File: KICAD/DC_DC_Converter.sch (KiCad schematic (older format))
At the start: 0 parts

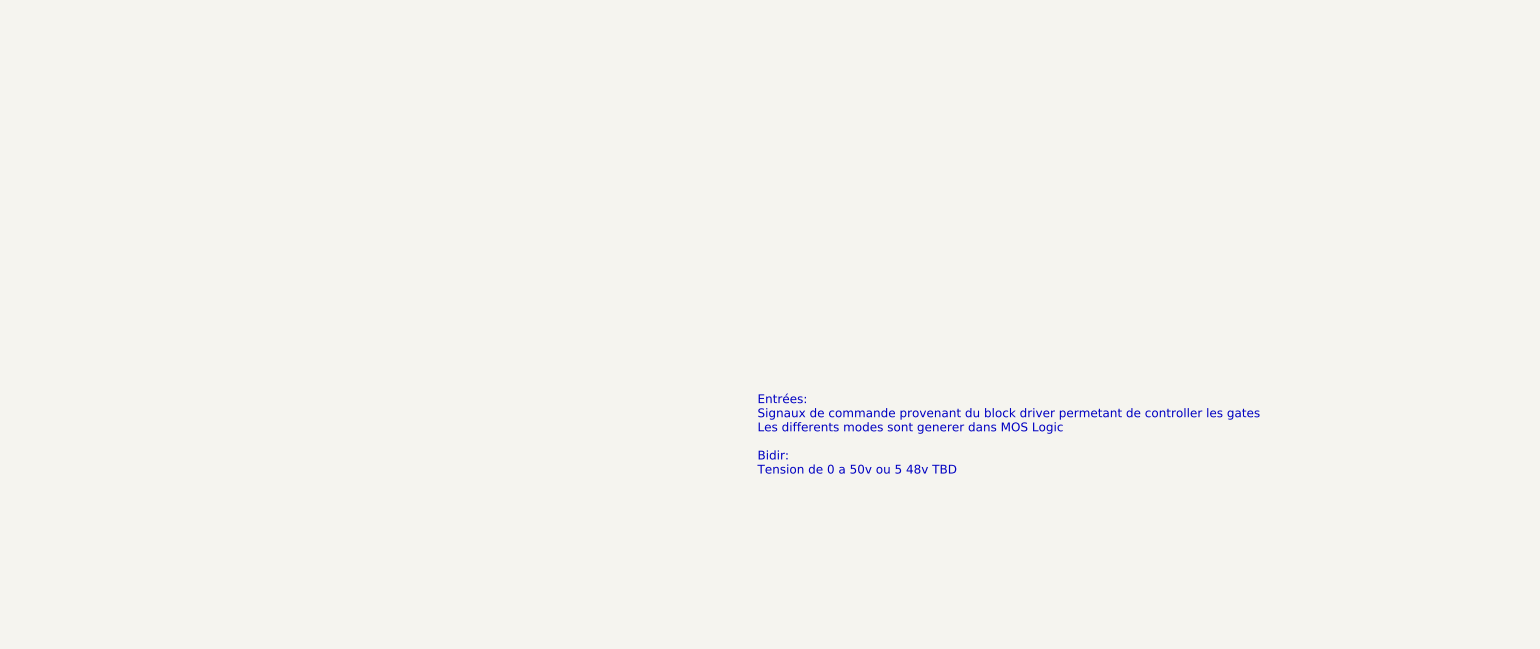
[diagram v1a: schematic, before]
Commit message: labels dans les blocks
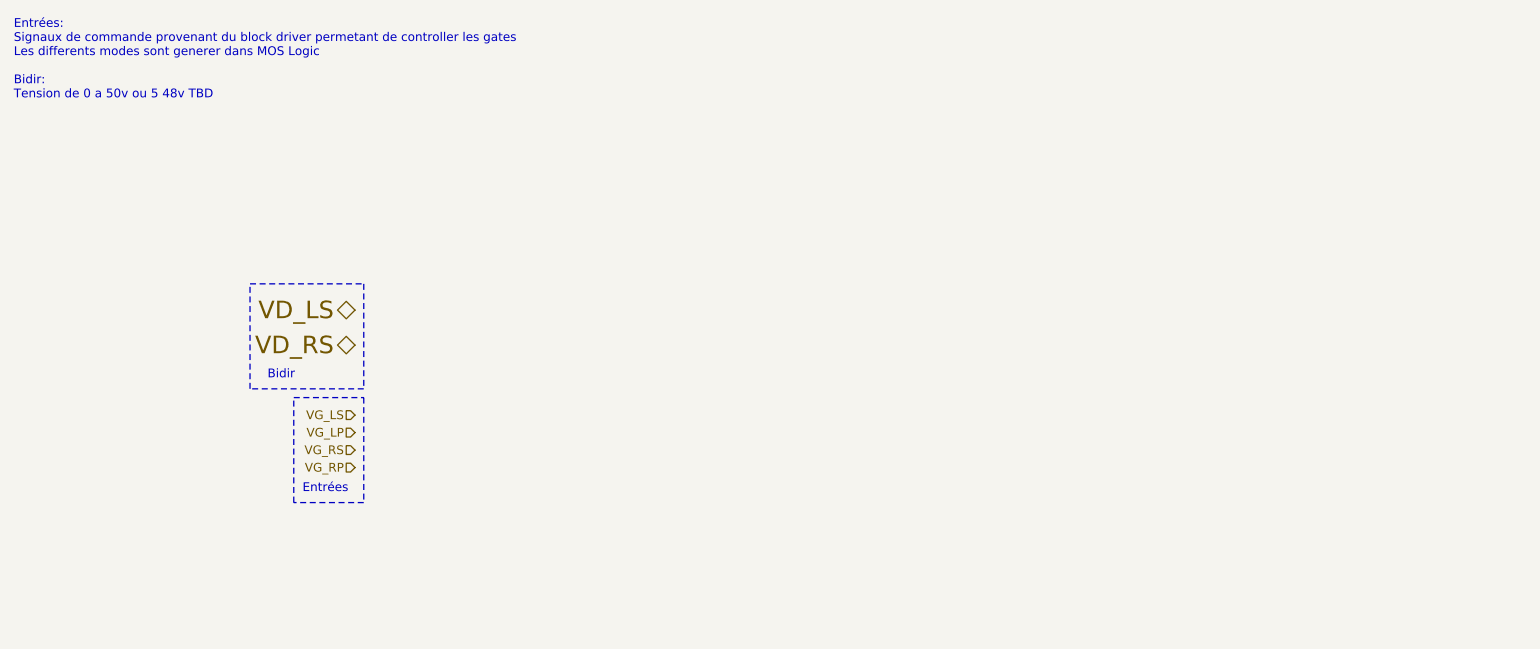
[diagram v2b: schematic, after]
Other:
- note added: "Bidir"
- note added: "Entrées"
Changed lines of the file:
@@
 Comment4 ""
 $EndDescr
-Text Notes 4800 3150 0    50   ~ 0
+Text Notes 550  1000 0    50   ~ 0
 Entrées:\nSignaux de commande provenant du block driver permetant de controller les gates\nLes differents modes sont generer dans MOS Logic\n\nBidir:\nTension de 0 a 50v ou 5 48v TBD\n
+Text HLabel 2500 2200 0    100  BiDi ~ 0
+VD_LS
+Text HLabel 2500 2400 0    100  BiDi ~ 0
+VD_RS
+Text HLabel 2500 2800 0    50   Input ~ 0
+VG_LS
+Text HLabel 2500 2900 0    50   Input ~ 0
+VG_LP
+Text HLabel 2500 3000 0    50   Input ~ 0
+VG_RS
+Text HLabel 2500 3100 0    50   Input ~ 0
+VG_RP
+Text Notes 2200 3250 0    50   ~ 0
+Entrées
+Text Notes 2000 2600 0    50   ~ 0
+Bidir
+Wire Notes Line
+	2550 3300 2150 3300
+Wire Notes Line
+	2150 3300 2150 2700
+Wire Notes Line
+	2150 2700 2550 2700
+Wire Notes Line
+	2550 2700 2550 3300
+Wire Notes Line
+	2550 2650 1900 2650
+Wire Notes Line
+	1900 2650 1900 2050
+Wire Notes Line
+	1900 2050 2550 2050
+Wire Notes Line
+	2550 2050 2550 2650
 $EndSCHEMATC

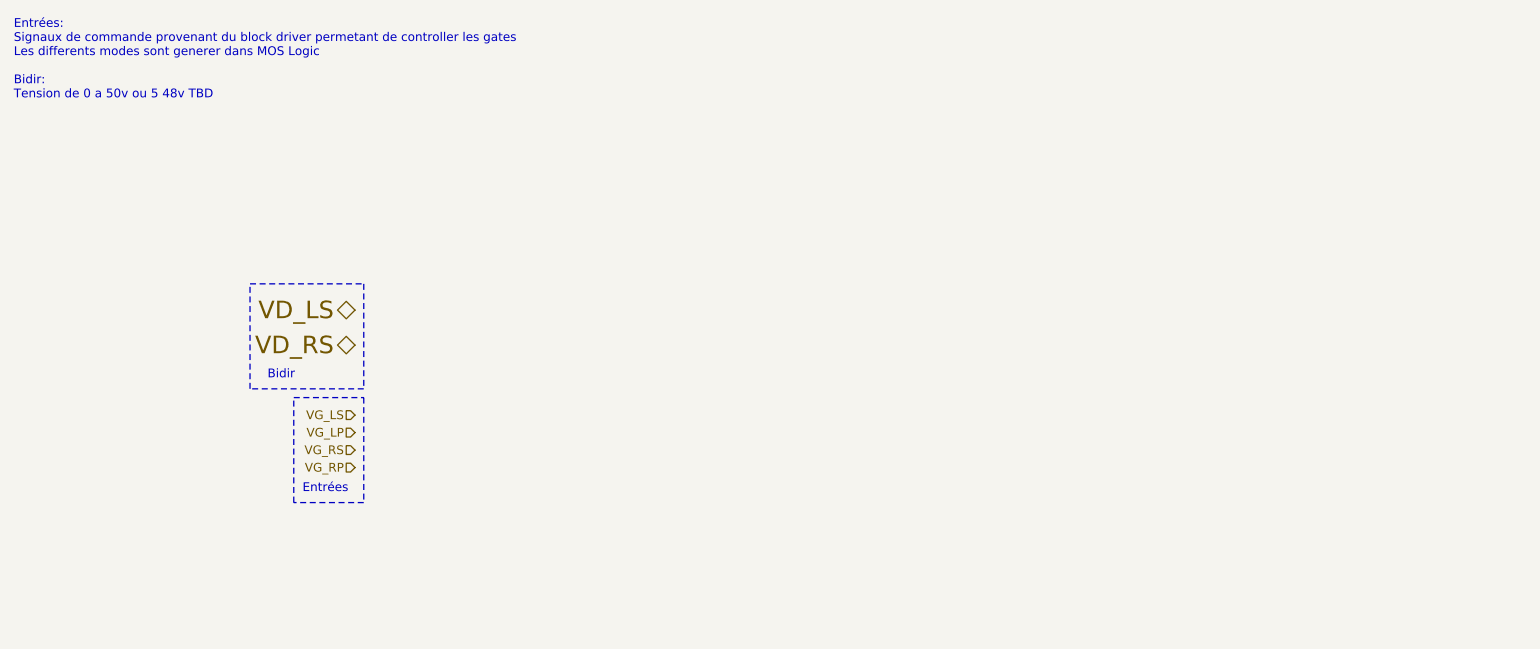
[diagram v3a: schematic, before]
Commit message: added ina240 sim + drawed protect and DC-DC chopper
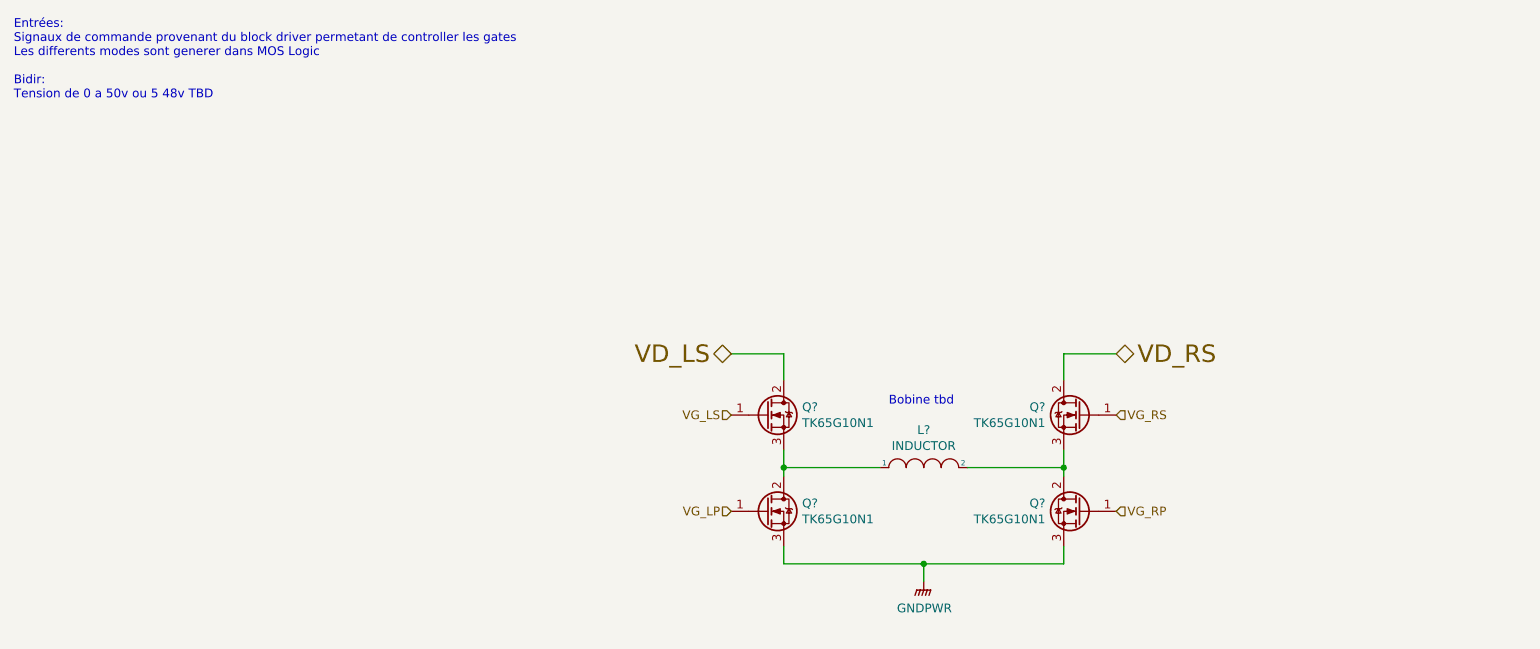
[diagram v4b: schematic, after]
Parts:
- added L?: INDUCTOR, symbol pspice:INDUCTOR
- added Q? (x4): TK65G10N1, symbol Device:Q_NMOS_GDS
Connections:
- net VD_LS: now also Q?.2 (D)
- net VD_RS: now also Q?.2 (D)
- net VG_LP: now also Q?.1 (G)
- net VG_LS: now also Q?.1 (G)
- net VG_RP: now also Q?.1 (G)
- net VG_RS: now also Q?.1 (G)
- new net: L?.1, Q?.2 (D), Q?.3 (S)
- new net: L?.2, Q?.2 (D), Q?.3 (S)
- new net GNDPWR: Q?.3 (S), Q?.3 (S)
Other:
- note added: "Bobine tbd"
- note removed: "Bidir"
- note removed: "Entrées"
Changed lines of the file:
@@
 Rev ""
 Comp "ALEEA"
-Comment1 ""
+Comment1 "Dessin : Guillaume Arthaud"
 Comment2 ""
 Comment3 ""
@@
 Text Notes 550  1000 0    50   ~ 0
 Entrées:\nSignaux de commande provenant du block driver permetant de controller les gates\nLes differents modes sont generer dans MOS Logic\n\nBidir:\nTension de 0 a 50v ou 5 48v TBD\n
-Text HLabel 2500 2200 0    100  BiDi ~ 0
+Text HLabel 4650 2450 0    100  BiDi ~ 0
 VD_LS
-Text HLabel 2500 2400 0    100  BiDi ~ 0
+Text HLabel 6850 2450 2    100  BiDi ~ 0
 VD_RS
-Text HLabel 2500 2800 0    50   Input ~ 0
+Text HLabel 4650 2800 0    50   Input ~ 0
 VG_LS
-Text HLabel 2500 2900 0    50   Input ~ 0
+Text HLabel 4650 3350 0    50   Input ~ 0
 VG_LP
-Text HLabel 2500 3000 0    50   Input ~ 0
+Text HLabel 6850 2800 2    50   Input ~ 0
 VG_RS
-Text HLabel 2500 3100 0    50   Input ~ 0
+Text HLabel 6850 3350 2    50   Input ~ 0
 VG_RP
-Text Notes 2200 3250 0    50   ~ 0
-Entrées
-Text Notes 2000 2600 0    50   ~ 0
-Bidir
-Wire Notes Line
-	2550 3300 2150 3300
-Wire Notes Line
-	2150 3300 2150 2700
-Wire Notes Line
-	2150 2700 2550 2700
-Wire Notes Line
-	2550 2700 2550 3300
-Wire Notes Line
-	2550 2650 1900 2650
-Wire Notes Line
-	1900 2650 1900 2050
-Wire Notes Line
-	1900 2050 2550 2050
-Wire Notes Line
-	2550 2050 2550 2650
+$Comp
+L Device:Q_NMOS_GDS Q?
+U 1 1 610E334F
+P 4850 2800
+F 0 "Q?" H 5055 2846 50  0000 L CNN
+F 1 "TK65G10N1" H 5055 2755 50  0000 L CNN
+F 2 "" H 5050 2900 50  0001 C CNN
+F 3 "~" H 4850 2800 50  0001 C CNN
+	1    4850 2800
+	1    0    0    -1
+$EndComp
+$Comp
+L Device:Q_NMOS_GDS Q?
+U 1 1 610EEE2E
+P 4850 3350
+F 0 "Q?" H 5055 3396 50  0000 L CNN
+F 1 "TK65G10N1" H 5055 3305 50  0000 L CNN
+F 2 "" H 5050 3450 50  0001 C CNN
+F 3 "~" H 4850 3350 50  0001 C CNN
+	1    4850 3350
+	1    0    0    -1
+$EndComp
+$Comp
+L Device:Q_NMOS_GDS Q?
+U 1 1 610F207F
+P 6650 2800
+F 0 "Q?" H 6855 2846 50  0000 L CNN
+F 1 "TK65G10N1" H 6855 2755 50  0000 L CNN
+F 2 "" H 6850 2900 50  0001 C CNN
+F 3 "~" H 6650 2800 50  0001 C CNN
+	1    6650 2800
+	-1   0    0    -1
+$EndComp
+$Comp
+L Device:Q_NMOS_GDS Q?
+U 1 1 610F2085
+P 6650 3350
+F 0 "Q?" H 6855 3396 50  0000 L CNN
+F 1 "TK65G10N1" H 6855 3305 50  0000 L CNN
+F 2 "" H 6850 3450 50  0001 C CNN
+F 3 "~" H 6650 3350 50  0001 C CNN
+	1    6650 3350
+	-1   0    0    -1
+$EndComp
+Wire Wire Line
+	6550 3000 6550 3100
+Wire Wire Line
+	4950 3150 4950 3100
+Wire Wire Line
+	4950 3550 4950 3650
+Wire Wire Line
+	6550 3650 6550 3550
+$Comp
+L pspice:INDUCTOR L?
+U 1 1 610F3EF5
+P 5750 3100
+F 0 "L?" H 5750 3315 50  0000 C CNN
+F 1 "INDUCTOR" H 5750 3224 50  0000 C CNN
+F 2 "" H 5750 3100 50  0001 C CNN
+F 3 "~" H 5750 3100 50  0001 C CNN
+	1    5750 3100
+	1    0    0    -1
+$EndComp
+Wire Wire Line
+	4950 3650 5750 3650
+Wire Wire Line
+	5500 3100 4950 3100
+Connection ~ 4950 3100
+Wire Wire Line
+	4950 3100 4950 3000
+Wire Wire Line
+	6550 3100 6000 3100
+Connection ~ 6550 3100
+Wire Wire Line
+	6550 3100 6550 3150
+Wire Wire Line
+	4950 2600 4950 2450
+Wire Wire Line
+	4650 2450 4950 2450
+Wire Wire Line
+	6550 2600 6550 2450
+Wire Wire Line
+	6850 2450 6550 2450
+Text Notes 5550 2750 0    50   ~ 0
+Bobine tbd
+Wire Wire Line
+	5750 3750 5750 3650
+Connection ~ 5750 3650
+Wire Wire Line
+	5750 3650 6550 3650
+$Comp
+L power:GNDPWR #PWR?
+U 1 1 610FB372
+P 5750 3750
+F 0 "#PWR?" H 5750 3550 50  0001 C CNN
+F 1 "GNDPWR" H 5754 3596 50  0000 C CNN
+F 2 "" H 5750 3700 50  0001 C CNN
+F 3 "" H 5750 3700 50  0001 C CNN
+	1    5750 3750
+	1    0    0    -1
+$EndComp
 $EndSCHEMATC

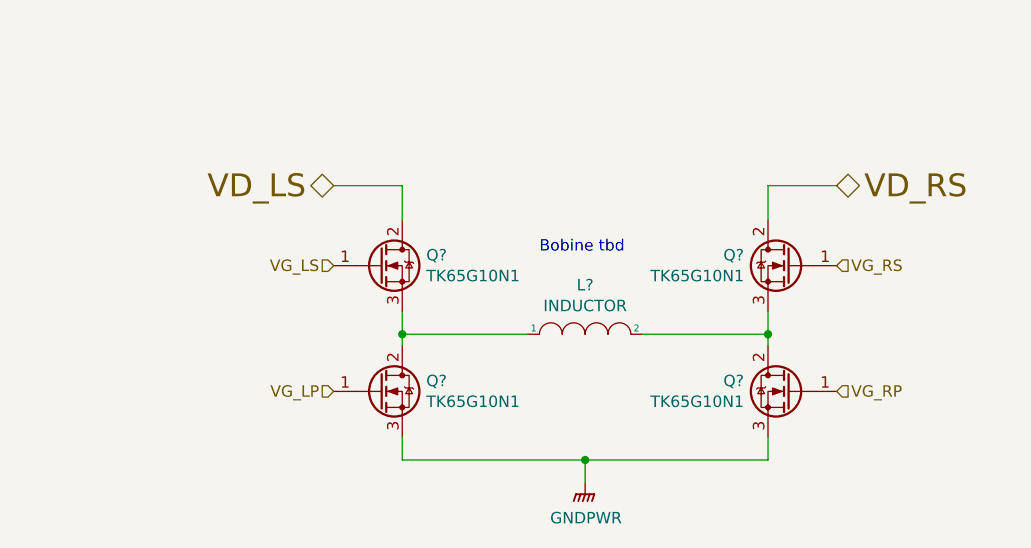
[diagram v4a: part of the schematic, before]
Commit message: minors edits + 7v rail
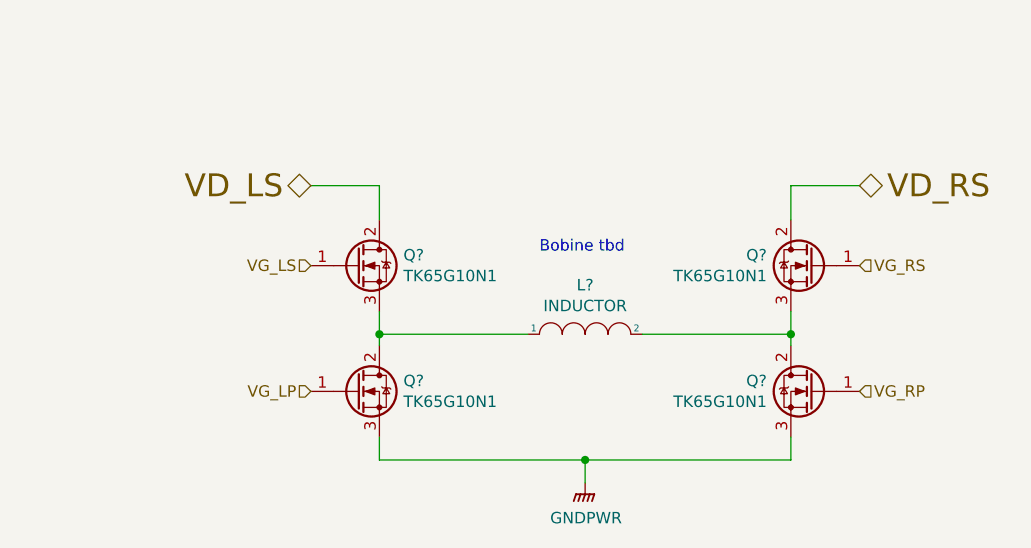
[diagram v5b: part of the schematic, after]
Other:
- moved on the sheet: Q?
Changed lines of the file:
@@
 Text Notes 550  1000 0    50   ~ 0
 Entrées:\nSignaux de commande provenant du block driver permetant de controller les gates\nLes differents modes sont generer dans MOS Logic\n\nBidir:\nTension de 0 a 50v ou 5 48v TBD\n
-Text HLabel 4650 2450 0    100  BiDi ~ 0
+Text HLabel 4550 2450 0    100  BiDi ~ 0
 VD_LS
-Text HLabel 6850 2450 2    100  BiDi ~ 0
+Text HLabel 6950 2450 2    100  BiDi ~ 0
 VD_RS
-Text HLabel 4650 2800 0    50   Input ~ 0
+Text HLabel 4550 2800 0    50   Input ~ 0
 VG_LS
-Text HLabel 4650 3350 0    50   Input ~ 0
+Text HLabel 4550 3350 0    50   Input ~ 0
 VG_LP
-Text HLabel 6850 2800 2    50   Input ~ 0
+Text HLabel 6950 2800 2    50   Input ~ 0
 VG_RS
-Text HLabel 6850 3350 2    50   Input ~ 0
+Text HLabel 6950 3350 2    50   Input ~ 0
 VG_RP
 $Comp
 L Device:Q_NMOS_GDS Q?
 U 1 1 610E334F
-P 4850 2800
-F 0 "Q?" H 5055 2846 50  0000 L CNN
-F 1 "TK65G10N1" H 5055 2755 50  0000 L CNN
-F 2 "" H 5050 2900 50  0001 C CNN
-F 3 "~" H 4850 2800 50  0001 C CNN
-	1    4850 2800
+P 4750 2800
+F 0 "Q?" H 4955 2846 50  0000 L CNN
+F 1 "TK65G10N1" H 4955 2755 50  0000 L CNN
+F 2 "" H 4950 2900 50  0001 C CNN
+F 3 "~" H 4750 2800 50  0001 C CNN
+	1    4750 2800
 	1    0    0    -1
 $EndComp
@@
 L Device:Q_NMOS_GDS Q?
 U 1 1 610EEE2E
-P 4850 3350
-F 0 "Q?" H 5055 3396 50  0000 L CNN
-F 1 "TK65G10N1" H 5055 3305 50  0000 L CNN
-F 2 "" H 5050 3450 50  0001 C CNN
-F 3 "~" H 4850 3350 50  0001 C CNN
-	1    4850 3350
+P 4750 3350
+F 0 "Q?" H 4955 3396 50  0000 L CNN
+F 1 "TK65G10N1" H 4955 3305 50  0000 L CNN
+F 2 "" H 4950 3450 50  0001 C CNN
+F 3 "~" H 4750 3350 50  0001 C CNN
+	1    4750 3350
 	1    0    0    -1
 $EndComp
@@
 L Device:Q_NMOS_GDS Q?
 U 1 1 610F207F
-P 6650 2800
-F 0 "Q?" H 6855 2846 50  0000 L CNN
-F 1 "TK65G10N1" H 6855 2755 50  0000 L CNN
-F 2 "" H 6850 2900 50  0001 C CNN
-F 3 "~" H 6650 2800 50  0001 C CNN
-	1    6650 2800
+P 6750 2800
+F 0 "Q?" H 6955 2846 50  0000 L CNN
+F 1 "TK65G10N1" H 6955 2755 50  0000 L CNN
+F 2 "" H 6950 2900 50  0001 C CNN
+F 3 "~" H 6750 2800 50  0001 C CNN
+	1    6750 2800
 	-1   0    0    -1
 $EndComp
@@
 L Device:Q_NMOS_GDS Q?
 U 1 1 610F2085
-P 6650 3350
-F 0 "Q?" H 6855 3396 50  0000 L CNN
-F 1 "TK65G10N1" H 6855 3305 50  0000 L CNN
-F 2 "" H 6850 3450 50  0001 C CNN
-F 3 "~" H 6650 3350 50  0001 C CNN
-	1    6650 3350
+P 6750 3350
+F 0 "Q?" H 6955 3396 50  0000 L CNN
+F 1 "TK65G10N1" H 6955 3305 50  0000 L CNN
+F 2 "" H 6950 3450 50  0001 C CNN
+F 3 "~" H 6750 3350 50  0001 C CNN
+	1    6750 3350
 	-1   0    0    -1
 $EndComp
 Wire Wire Line
-	6550 3000 6550 3100
+	6650 3000 6650 3100
 Wire Wire Line
-	4950 3150 4950 3100
+	4850 3150 4850 3100
 Wire Wire Line
-	4950 3550 4950 3650
+	4850 3550 4850 3650
 Wire Wire Line
-	6550 3650 6550 3550
+	6650 3650 6650 3550
 $Comp
 L pspice:INDUCTOR L?
@@
 $EndComp
 Wire Wire Line
-	4950 3650 5750 3650
+	4850 3650 5750 3650
 Wire Wire Line
-	5500 3100 4950 3100
-Connection ~ 4950 3100
+	5500 3100 4850 3100
+Connection ~ 4850 3100
 Wire Wire Line
-	4950 3100 4950 3000
+	4850 3100 4850 3000
 Wire Wire Line
-	6550 3100 6000 3100
-Connection ~ 6550 3100
+	6650 3100 6000 3100
+Connection ~ 6650 3100
 Wire Wire Line
-	6550 3100 6550 3150
+	6650 3100 6650 3150
 Wire Wire Line
-	4950 2600 4950 2450
+	4850 2600 4850 2450
 Wire Wire Line
-	4650 2450 4950 2450
+	4550 2450 4850 2450
 Wire Wire Line
-	6550 2600 6550 2450
+	6650 2600 6650 2450
 Wire Wire Line
-	6850 2450 6550 2450
+	6950 2450 6650 2450
 Text Notes 5550 2750 0    50   ~ 0
 Bobine tbd
@@
 Connection ~ 5750 3650
 Wire Wire Line
-	5750 3650 6550 3650
+	5750 3650 6650 3650
 $Comp
 L power:GNDPWR #PWR?
